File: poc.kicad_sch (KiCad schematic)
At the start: 24 parts, among them J1 USB_C_Receptacle_USB2.0_14P, J2 Conn_01x04_Pin, SW1 SW_Push, SW2 SW_Push, U1 ESP32-S3-WROOM-1, U2 AP7361C-33E, U3 USBLC6-2SC6

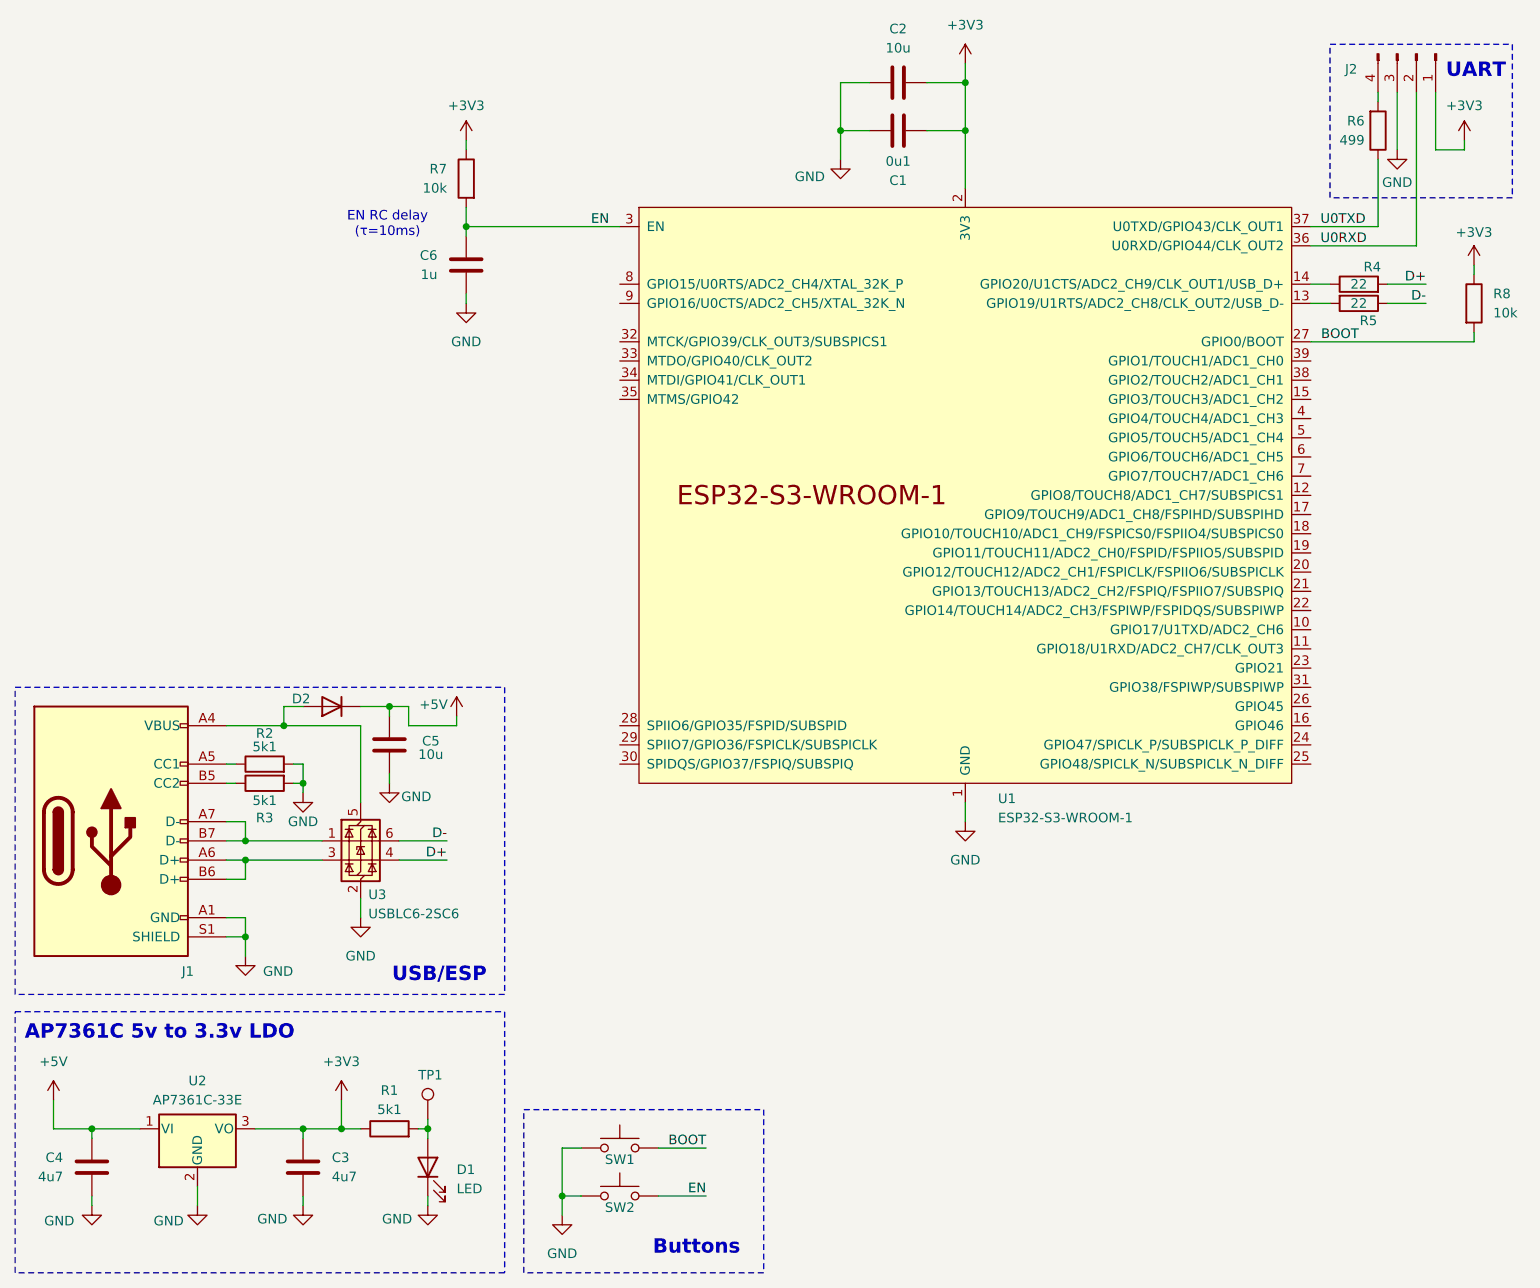
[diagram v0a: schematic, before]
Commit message: POC(schem): add dip switches
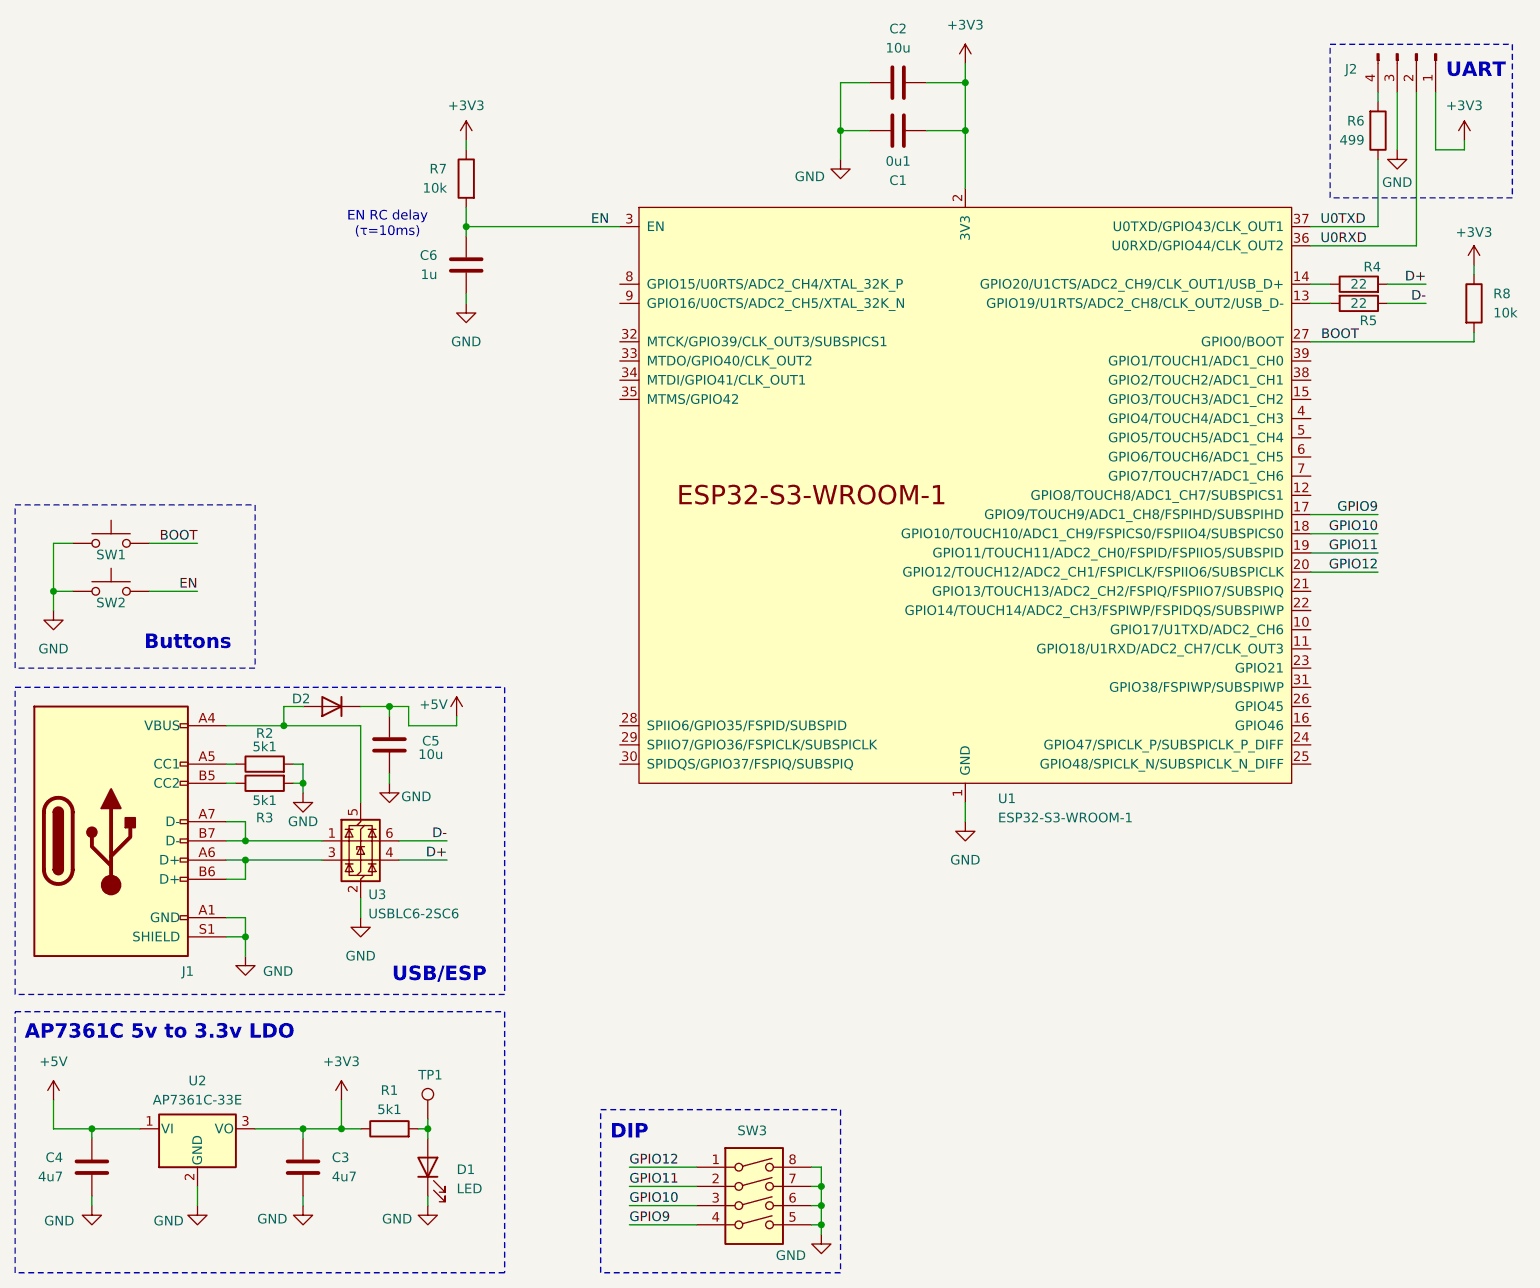
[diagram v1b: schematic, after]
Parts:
- added SW3: SW_DIP_x04, Button_Switch_THT:SW_DIP_SPSTx04_Slide_9.78x12.34mm_W7.62mm_P2.54mm, symbol Switch:SW_DIP_x04
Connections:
- net GND: now also SW3.5, SW3.6, SW3.7, SW3.8
- net GPIO9: now reaches U1.17 (GPIO9/TOUCH9/ADC1_CH8/FSPIHD/SUBSPIHD)
- net GPIO9: now also SW3.4
- net GPIO10: now reaches U1.18 (GPIO10/TOUCH10/ADC1_CH9/FSPICS0/FSPIIO4/SUBSPICS0)
- net GPIO10: now also SW3.3
- net GPIO11: now reaches U1.19 (GPIO11/TOUCH11/ADC2_CH0/FSPID/FSPIIO5/SUBSPID)
- net GPIO11: now also SW3.2
- net GPIO12: now reaches U1.20 (GPIO12/TOUCH12/ADC2_CH1/FSPICLK/FSPIIO6/SUBSPICLK)
- net GPIO12: now also SW3.1
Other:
- note added: "DIP"
- moved on the sheet: SW1, SW2
